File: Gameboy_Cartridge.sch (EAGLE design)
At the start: 3 parts

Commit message: add mcu design
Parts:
- added U$2: STM32F405RG, gameboy:STM32F405RG
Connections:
- new net N$1: U$2.VDD@1, U$2.VDD@2, U$2.VDD@3, U$2.VDD@4
- new net N$2: U$2.VSS@1, U$2.VSS@2
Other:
- moved on the sheet: C1, R1
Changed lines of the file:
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@@
 <?xml version="1.0" encoding="utf-8"?>
 <!DOCTYPE eagle SYSTEM "eagle.dtd">
-<eagle version="7.5.0">
+<eagle version="8.5.1">
 <drawing>
 <settings>
 <setting alwaysvectorfont="no"/>
+<setting keepoldvectorfont="yes"/>
 <setting verticaltext="up"/>
 </settings>
@@
 <part name="R1" library="resistor" deviceset="R-US_" device="M0805" value="47K"/>
 <part name="C1" library="resistor" deviceset="C-EU" device="C0805" value="20nF"/>
+<part name="U$2" library="gameboy" deviceset="STM32F405RG" device=""/>
 </parts>
 <sheets>
@@
 <instances>
 <instance part="U$1" gate="G$1" x="-10.16" y="50.8"/>
-<instance part="R1" gate="G$1" x="55.88" y="129.54"/>
-<instance part="C1" gate="G$1" x="55.88" y="116.84" rot="R90"/>
+<instance part="R1" gate="G$1" x="187.96" y="233.68"/>
+<instance part="C1" gate="G$1" x="187.96" y="220.98" rot="R90"/>
+<instance part="U$2" gate="G$1" x="33.02" y="167.64"/>
 </instances>
 <busses>
@@
 <segment>
 <pinref part="R1" gate="G$1" pin="2"/>
-<wire x1="60.96" y1="129.54" x2="63.5" y2="129.54" width="0.1524" layer="91"/>
-<label x="63.5" y="129.54" size="1.778" layer="95"/>
+<wire x1="193.04" y1="233.68" x2="195.58" y2="233.68" width="0.1524" layer="91"/>
+<label x="195.58" y="233.68" size="1.778" layer="95"/>
+<label x="25.4" y="238.76" size="1.778" layer="95"/>
 </segment>
 <segment>
 <pinref part="C1" gate="G$1" pin="1"/>
-<wire x1="53.34" y1="116.84" x2="45.72" y2="116.84" width="0.1524" layer="91"/>
-<label x="45.72" y="116.84" size="1.778" layer="95"/>
+<wire x1="185.42" y1="220.98" x2="177.8" y2="220.98" width="0.1524" layer="91"/>
+<label x="177.8" y="220.98" size="1.778" layer="95"/>
 </segment>
 </net>
@@
 <segment>
 <pinref part="C1" gate="G$1" pin="2"/>
-<wire x1="60.96" y1="116.84" x2="63.5" y2="116.84" width="0.1524" layer="91"/>
-<label x="63.5" y="116.84" size="1.778" layer="95"/>
+<wire x1="193.04" y1="220.98" x2="195.58" y2="220.98" width="0.1524" layer="91"/>
+<label x="195.58" y="220.98" size="1.778" layer="95"/>
+<label x="27.94" y="104.14" size="1.778" layer="95"/>
 </segment>
 </net>
@@
 <segment>
 <pinref part="R1" gate="G$1" pin="1"/>
-<wire x1="50.8" y1="129.54" x2="45.72" y2="129.54" width="0.1524" layer="91"/>
-<label x="45.72" y="129.54" size="1.778" layer="95"/>
+<wire x1="182.88" y1="233.68" x2="177.8" y2="233.68" width="0.1524" layer="91"/>
+<label x="177.8" y="233.68" size="1.778" layer="95"/>
 </segment>
 </net>
+<net name="N$1" class="0">
+<segment>
+<pinref part="U$2" gate="G$1" pin="VDD@1"/>
+<wire x1="25.4" y1="231.14" x2="25.4" y2="233.68" width="0.1524" layer="91"/>
+<wire x1="25.4" y1="233.68" x2="27.94" y2="233.68" width="0.1524" layer="91"/>
+<pinref part="U$2" gate="G$1" pin="VDD@4"/>
+<wire x1="27.94" y1="233.68" x2="30.48" y2="233.68" width="0.1524" layer="91"/>
+<wire x1="30.48" y1="233.68" x2="33.02" y2="233.68" width="0.1524" layer="91"/>
+<wire x1="33.02" y1="233.68" x2="33.02" y2="231.14" width="0.1524" layer="91"/>
+<pinref part="U$2" gate="G$1" pin="VDD@3"/>
+<wire x1="30.48" y1="231.14" x2="30.48" y2="233.68" width="0.1524" layer="91"/>
+<junction x="30.48" y="233.68"/>
+<pinref part="U$2" gate="G$1" pin="VDD@2"/>
+<wire x1="27.94" y1="231.14" x2="27.94" y2="233.68" width="0.1524" layer="91"/>
+<junction x="27.94" y="233.68"/>
+<wire x1="25.4" y1="233.68" x2="25.4" y2="238.76" width="0.1524" layer="91"/>
+<junction x="25.4" y="233.68"/>
+</segment>
+</net>
+<net name="N$2" class="0">
+<segment>
+<pinref part="U$2" gate="G$1" pin="VSS@1"/>
+<wire x1="27.94" y1="111.76" x2="27.94" y2="109.22" width="0.1524" layer="91"/>
+<wire x1="27.94" y1="109.22" x2="30.48" y2="109.22" width="0.1524" layer="91"/>
+<pinref part="U$2" gate="G$1" pin="VSS@2"/>
+<wire x1="30.48" y1="109.22" x2="30.48" y2="111.76" width="0.1524" layer="91"/>
+<wire x1="27.94" y1="109.22" x2="27.94" y2="104.14" width="0.1524" layer="91"/>
+</segment>
+</net>

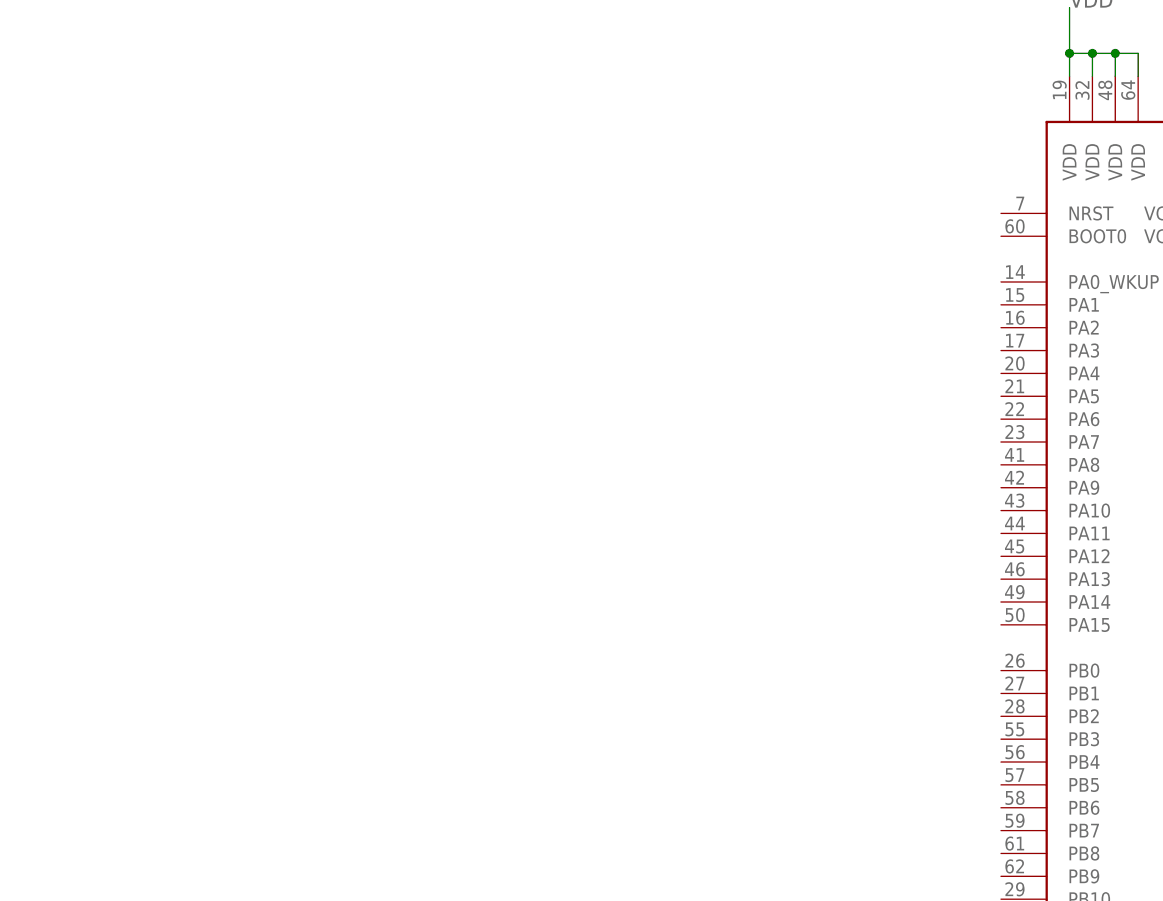
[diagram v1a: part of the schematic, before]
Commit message: add programming header
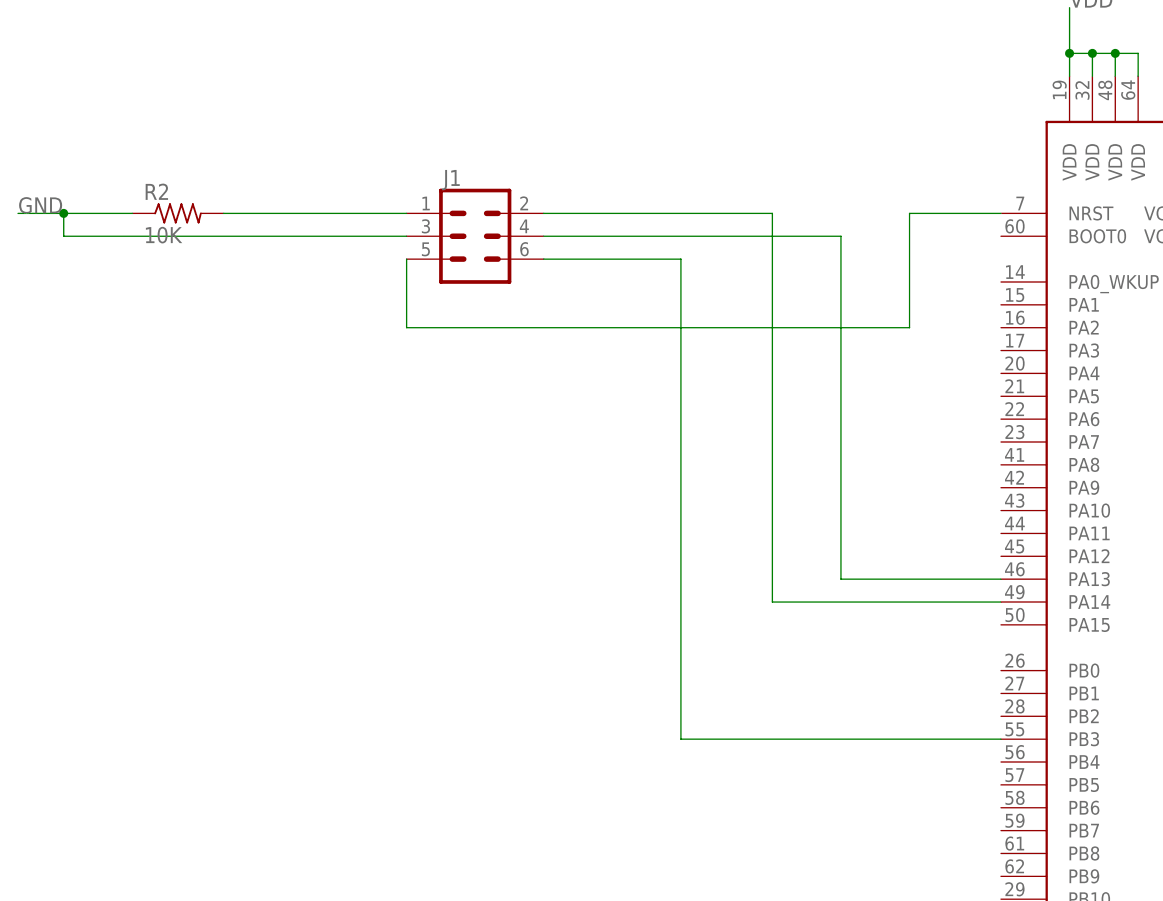
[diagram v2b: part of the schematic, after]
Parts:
- added J1: (no value), SparkFun-Connectors:CONN_03X2FEMALE_SMD
- added R2: 10K, resistor:R-US_M0805
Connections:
- new net N$3: J1.1, R2.2
- new net N$4: J1.3, R2.1
- new net N$5: J1.2, U$2.PA14
- new net N$7: J1.4, U$2.PA13
- new net N$8: J1.5, U$2.NRST
- new net N$9: J1.6, U$2.PB3

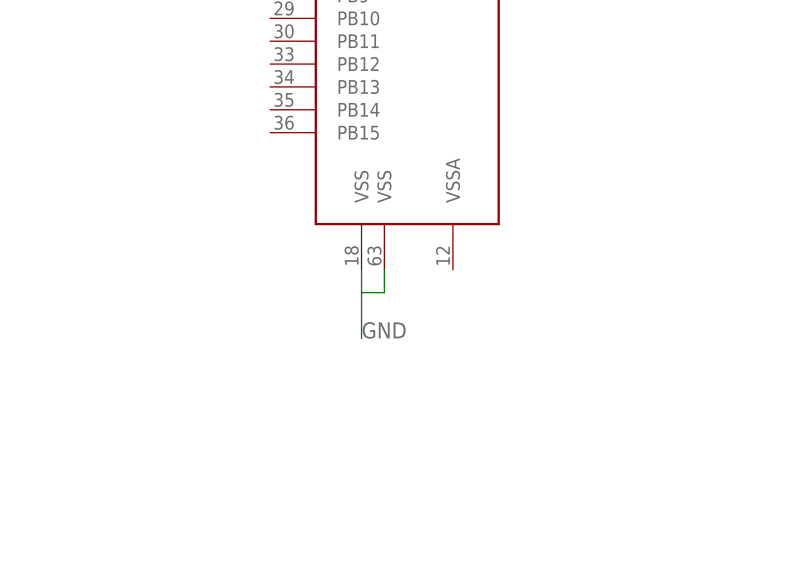
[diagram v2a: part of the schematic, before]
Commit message: connect mcu grounds
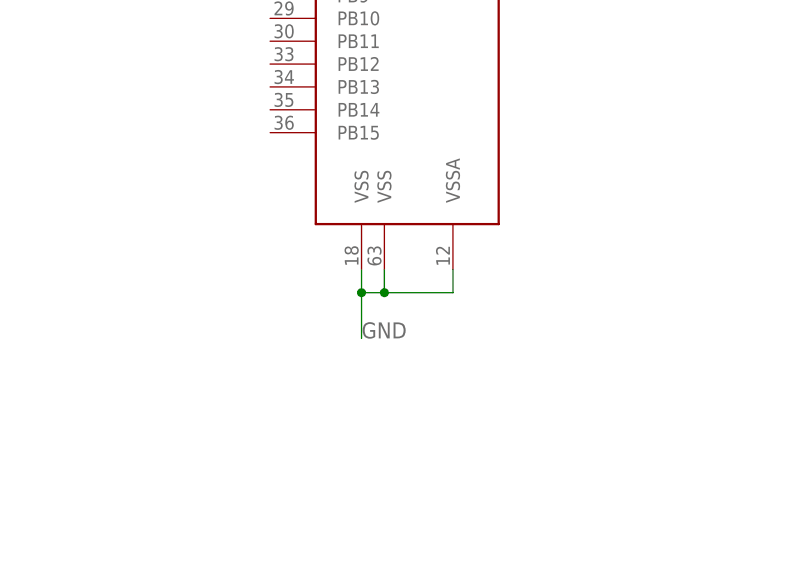
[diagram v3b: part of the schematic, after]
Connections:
- net N$2: now also U$2.VSSA
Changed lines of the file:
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@@
 <pinref part="U$2" gate="G$1" pin="VSS@1"/>
 <wire x1="27.94" y1="111.76" x2="27.94" y2="109.22" width="0.1524" layer="91"/>
-<wire x1="27.94" y1="109.22" x2="30.48" y2="109.22" width="0.1524" layer="91"/>
 <pinref part="U$2" gate="G$1" pin="VSS@2"/>
 <wire x1="30.48" y1="109.22" x2="30.48" y2="111.76" width="0.1524" layer="91"/>
 <wire x1="27.94" y1="109.22" x2="27.94" y2="104.14" width="0.1524" layer="91"/>
+<pinref part="U$2" gate="G$1" pin="VSSA"/>
+<wire x1="38.1" y1="111.76" x2="38.1" y2="109.22" width="0.1524" layer="91"/>
+<wire x1="38.1" y1="109.22" x2="30.48" y2="109.22" width="0.1524" layer="91"/>
+<junction x="30.48" y="109.22"/>
+<wire x1="30.48" y1="109.22" x2="27.94" y2="109.22" width="0.1524" layer="91"/>
+<junction x="27.94" y="109.22"/>
 </segment>
 </net>

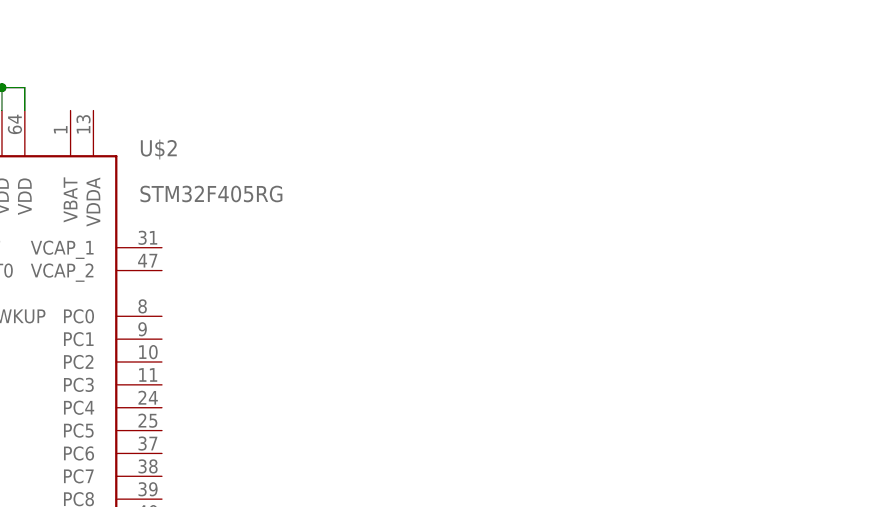
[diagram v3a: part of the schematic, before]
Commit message: add VCAPs
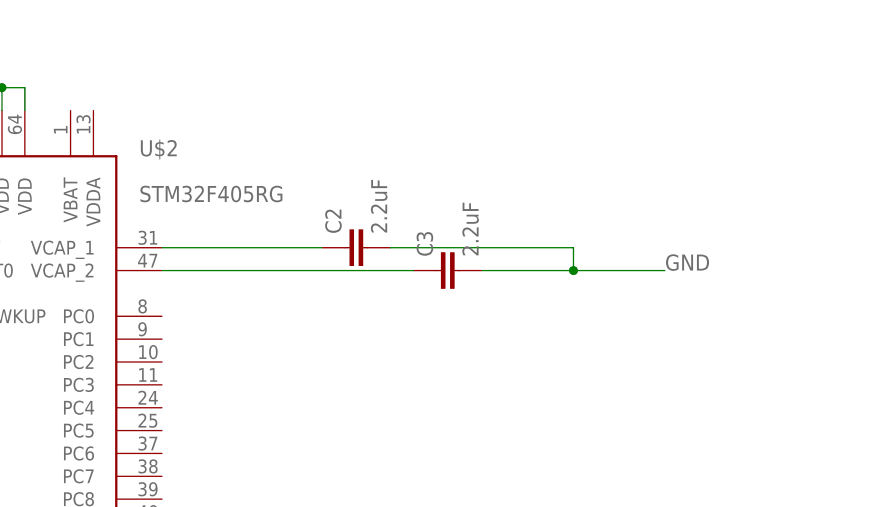
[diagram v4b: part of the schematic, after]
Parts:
- added C2, C3: 2.2uF, resistor:C-EUC0805
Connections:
- new net N$10: C2.1, U$2.VCAP_1
- new net N$11: C3.1, U$2.VCAP_2
- new net N$12: C2.2, C3.2
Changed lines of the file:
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@@
 <part name="J1" library="SparkFun-Connectors" library_urn="urn:adsk.eagle:library:513" deviceset="CONN_03X2" device="FEMALE_SMD" package3d_urn="urn:adsk.eagle:package:38267/1"/>
 <part name="R2" library="resistor" deviceset="R-US_" device="M0805" value="10K"/>
+<part name="C2" library="resistor" deviceset="C-EU" device="C0805" value="2.2uF"/>
+<part name="C3" library="resistor" deviceset="C-EU" device="C0805" value="2.2uF"/>
 </parts>
 <sheets>
@@
 <instance part="J1" gate="G$1" x="-40.64" y="213.36"/>
 <instance part="R2" gate="G$1" x="-73.66" y="215.9"/>
+<instance part="C2" gate="G$1" x="68.58" y="215.9" rot="R90"/>
+<instance part="C3" gate="G$1" x="78.74" y="213.36" rot="R90"/>
 </instances>
 <busses>
@@
 <label x="27.94" y="104.14" size="1.778" layer="95"/>
 <label x="-91.44" y="215.9" size="1.778" layer="95"/>
+<label x="104.14" y="213.36" size="1.778" layer="95"/>
 </segment>
 </net>
@@
 </segment>
 </net>
+<net name="N$10" class="0">
+<segment>
+<pinref part="C2" gate="G$1" pin="1"/>
+<pinref part="U$2" gate="G$1" pin="VCAP_1"/>
+<wire x1="66.04" y1="215.9" x2="48.26" y2="215.9" width="0.1524" layer="91"/>
+</segment>
+</net>
+<net name="N$11" class="0">
+<segment>
+<pinref part="U$2" gate="G$1" pin="VCAP_2"/>
+<pinref part="C3" gate="G$1" pin="1"/>
+<wire x1="48.26" y1="213.36" x2="76.2" y2="213.36" width="0.1524" layer="91"/>
+</segment>
+</net>
+<net name="N$12" class="0">
+<segment>
+<pinref part="C3" gate="G$1" pin="2"/>
+<wire x1="83.82" y1="213.36" x2="93.98" y2="213.36" width="0.1524" layer="91"/>
+<wire x1="93.98" y1="213.36" x2="93.98" y2="215.9" width="0.1524" layer="91"/>
+<pinref part="C2" gate="G$1" pin="2"/>
+<wire x1="93.98" y1="215.9" x2="73.66" y2="215.9" width="0.1524" layer="91"/>
+<wire x1="93.98" y1="213.36" x2="104.14" y2="213.36" width="0.1524" layer="91"/>
+<junction x="93.98" y="213.36"/>
+</segment>
+</net>
